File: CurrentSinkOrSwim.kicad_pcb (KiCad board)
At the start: 2 copper layers, 41.7 x 47.8 mm, 22 parts, among them P1 HEATSINK, P101 CONN_01X02, P102 CONN_01X03, P103 CONN_01X02, Q401 BUK9575, U201 LMV358, U301 LM2931

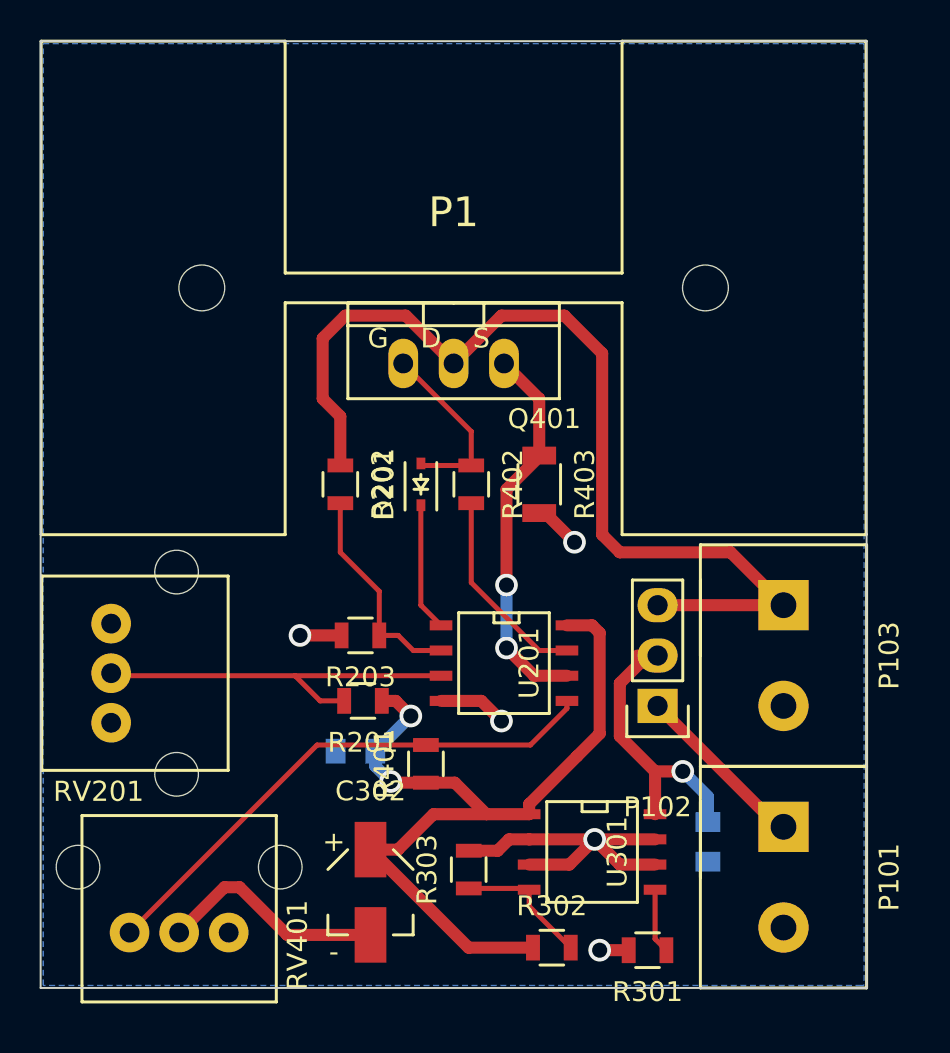
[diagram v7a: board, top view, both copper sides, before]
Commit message: fixed edge cut
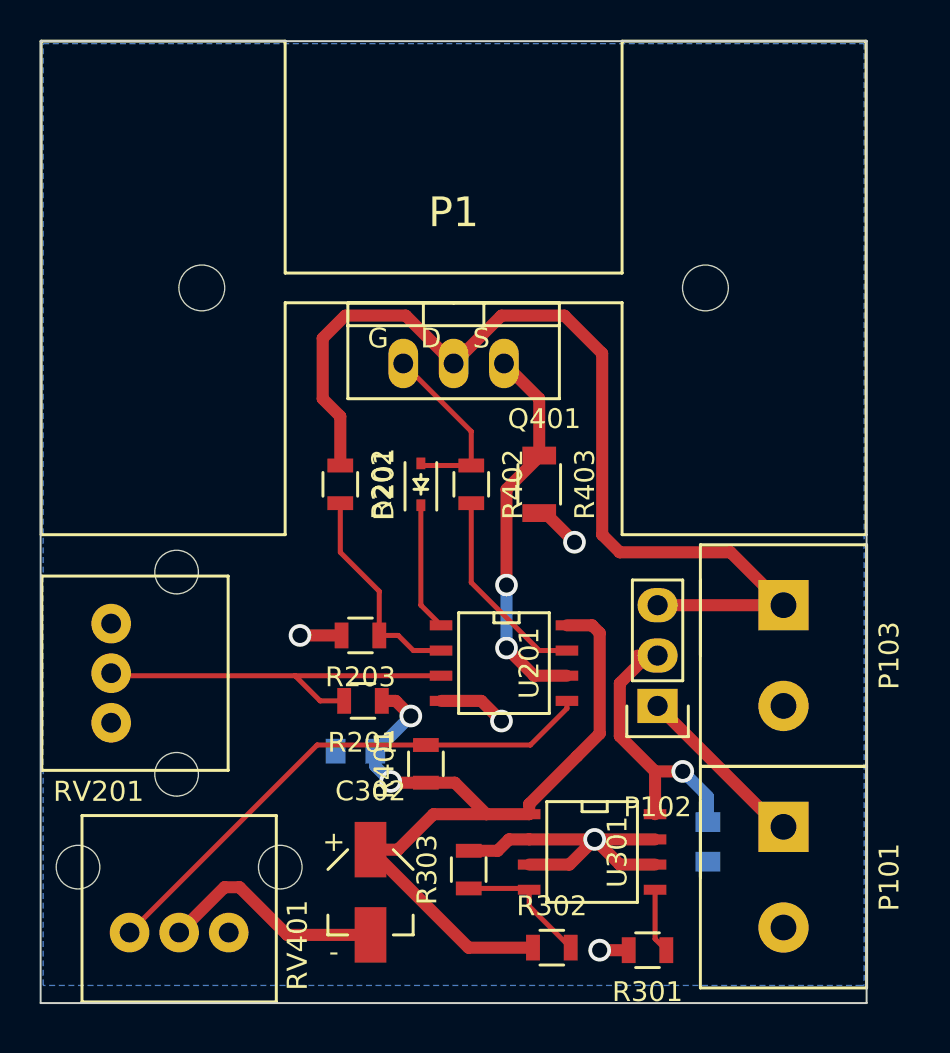
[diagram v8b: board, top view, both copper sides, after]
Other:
- board size 41.7 x 47.8 mm -> 41.7 x 48.5 mm
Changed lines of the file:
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@@
   )
   (gr_line (start 147.828 35.814) (end 106.172 35.814) (angle 90) (layer Edge.Cuts) (width 0.1))
-  (gr_line (start 147.828 83.566) (end 147.828 35.814) (angle 90) (layer Edge.Cuts) (width 0.1))
-  (gr_line (start 106.172 83.566) (end 147.828 83.566) (angle 90) (layer Edge.Cuts) (width 0.1))
-  (gr_line (start 106.172 35.814) (end 106.172 83.566) (angle 90) (layer Edge.Cuts) (width 0.1))
+  (gr_line (start 147.828 84.328) (end 147.828 35.814) (angle 90) (layer Edge.Cuts) (width 0.1))
+  (gr_line (start 106.172 84.328) (end 147.828 84.328) (angle 90) (layer Edge.Cuts) (width 0.1))
+  (gr_line (start 106.172 35.814) (end 106.172 84.328) (angle 90) (layer Edge.Cuts) (width 0.1))
   (segment (start 123.047 71.628) (end 123.063 71.628) (width 0.6096) (layer B.Cu) (net 1))
   (segment (start 123.063 71.628) (end 124.841 69.85) (width 0.6096) (layer B.Cu) (net 1))
